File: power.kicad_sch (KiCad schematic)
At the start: 20 parts, among them J1 1054500101, J2 S2B-PH-SM4-TB, U3 BQ25601, U4 XC6210B332MR, U5 XC6210B182MR

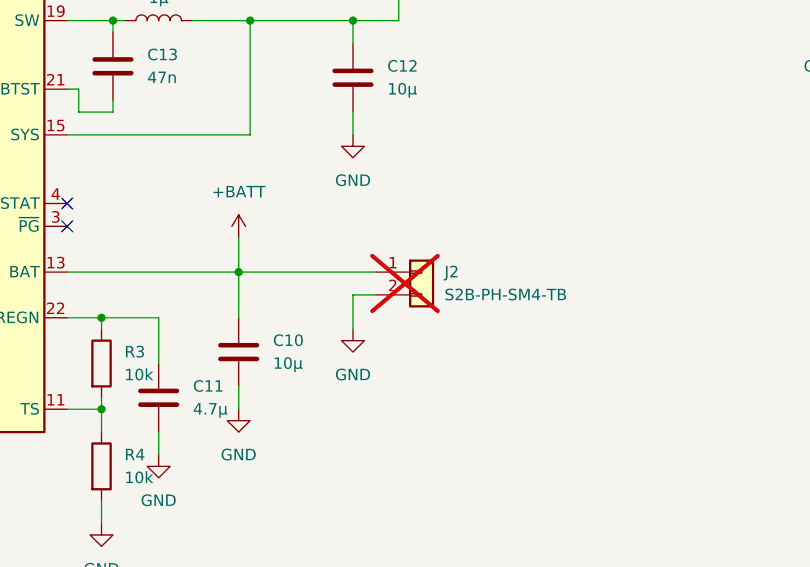
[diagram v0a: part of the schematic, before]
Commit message: Add battery connecter
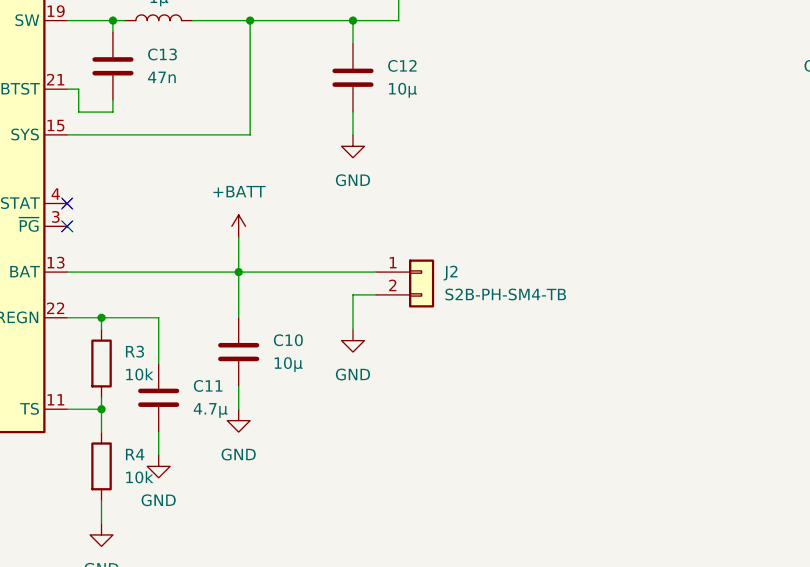
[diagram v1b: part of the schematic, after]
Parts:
- J2: JLCPCB Part # (none) -> C295747; manf# (none) -> S2B-PH-SM4-TB; now fitted; now in the parts list
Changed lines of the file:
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@@
 			)
 		)
+		(property "Sim.Enable" ""
+			(at 209.55 96.52 0)
+			(effects
+				(font
+					(size 1.27 1.27)
+				)
+				(hide yes)
+			)
+		)
 		(pin "3"
 		)
@@
 			)
 		)
+		(property "Sim.Enable" ""
+			(at 132.08 114.3 0)
+			(effects
+				(font
+					(size 1.27 1.27)
+				)
+				(hide yes)
+			)
+		)
 		(pin "2"
 		)
@@
 			)
 		)
+		(property "Sim.Enable" ""
+			(at 95.25 52.07 0)
+			(effects
+				(font
+					(size 1.27 1.27)
+				)
+				(hide yes)
+			)
+		)
 		(pin "1"
 		)
@@
 			)
 		)
+		(property "Sim.Enable" ""
+			(at 182.88 58.42 0)
+			(effects
+				(font
+					(size 1.27 1.27)
+				)
+				(hide yes)
+			)
+		)
 		(pin "2"
 		)
@@
 			)
 		)
+		(property "Sim.Enable" ""
+			(at 119.38 144.78 0)
+			(effects
+				(font
+					(size 1.27 1.27)
+				)
+				(hide yes)
+			)
+		)
 		(pin "2"
 		)
@@
 			)
 		)
+		(property "Sim.Enable" ""
+			(at 104.14 146.05 0)
+			(effects
+				(font
+					(size 1.27 1.27)
+				)
+				(hide yes)
+			)
+		)
 		(pin "2"
 		)
@@
 			)
 		)
+		(property "Sim.Enable" ""
+			(at 87.63 130.81 0)
+			(effects
+				(font
+					(size 1.27 1.27)
+				)
+				(hide yes)
+			)
+		)
 		(pin "1"
 		)
@@
 			)
 		)
+		(property "Sim.Enable" ""
+			(at 228.6 100.33 0)
+			(effects
+				(font
+					(size 1.27 1.27)
+				)
+				(hide yes)
+			)
+		)
 		(pin "2"
 		)
@@
 			)
 		)
+		(property "Sim.Enable" ""
+			(at 110.49 149.86 0)
+			(effects
+				(font
+					(size 1.27 1.27)
+				)
+				(hide yes)
+			)
+		)
 		(pin "2"
 		)
@@
 			)
 		)
+		(property "Sim.Enable" ""
+			(at 104.14 52.07 0)
+			(effects
+				(font
+					(size 1.27 1.27)
+				)
+				(hide yes)
+			)
+		)
 		(pin "1"
 		)
@@
 			)
 		)
+		(property "Sim.Enable" ""
+			(at 105.41 113.03 0)
+			(effects
+				(font
+					(size 1.27 1.27)
+				)
+				(hide yes)
+			)
+		)
 		(pin "2"
 		)
@@
 			)
 		)
+		(property "Sim.Enable" ""
+			(at 110.49 107.95 90)
+			(effects
+				(font
+					(size 1.27 1.27)
+				)
+				(hide yes)
+			)
+		)
 		(pin "1"
 		)
@@
 			)
 		)
+		(property "Sim.Enable" ""
+			(at 184.15 101.6 0)
+			(effects
+				(font
+					(size 1.27 1.27)
+				)
+				(hide yes)
+			)
+		)
 		(pin "2"
 		)
@@
 			)
 		)
+		(property "Sim.Enable" ""
+			(at 208.28 53.34 0)
+			(effects
+				(font
+					(size 1.27 1.27)
+				)
+				(hide yes)
+			)
+		)
 		(pin "3"
 		)
@@
 			)
 		)
+		(property "Sim.Enable" ""
+			(at 48.26 116.84 0)
+			(effects
+				(font
+					(size 1.27 1.27)
+				)
+				(hide yes)
+			)
+		)
 		(pin "2"
 		)
@@
 		(unit 1)
 		(exclude_from_sim no)
-		(in_bom no)
+		(in_bom yes)
 		(on_board yes)
-		(dnp yes)
+		(dnp no)
 		(fields_autoplaced yes)
 		(property "Reference" "J2"
@@
 			)
 		)
-		(property "JLCPCB Part #" ""
+		(property "JLCPCB Part #" "C295747"
 			(at 139.7 135.89 0)
 			(effects
@@
 			)
 		)
+		(property "Sim.Enable" ""
+			(at 139.7 135.89 0)
+			(effects
+				(font
+					(size 1.27 1.27)
+				)
+				(hide yes)
+			)
+		)
+		(property "manf#" "S2B-PH-SM4-TB"
+			(at 139.7 135.89 0)
+			(effects
+				(font
+					(size 1.27 1.27)
+				)
+				(hide yes)
+			)
+		)
 		(pin "1"
 		)
@@
 			)
 		)
+		(property "Sim.Enable" ""
+			(at 227.33 57.15 0)
+			(effects
+				(font
+					(size 1.27 1.27)
+				)
+				(hide yes)
+			)
+		)
 		(pin "2"
 		)
@@
 			)
 		)
+		(property "Sim.Enable" ""
+			(at 53.34 48.26 0)
+			(effects
+				(font
+					(size 1.27 1.27)
+				)
+				(hide yes)
+			)
+		)
 		(pin "S1"
 		)
@@
 			)
 		)
+		(property "Sim.Enable" ""
+			(at 104.14 157.48 0)
+			(effects
+				(font
+					(size 1.27 1.27)
+				)
+				(hide yes)
+			)
+		)
 		(pin "2"
 		)
@@
 			(at 66.04 157.48 0)
 			(effects
+				(font
+					(size 1.27 1.27)
+				)
+				(hide yes)
+			)
+		)
+		(property "Sim.Enable" ""
+			(at 66.04 157.48 0)
+			(effects

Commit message: some PCB correction
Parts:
- J1: value 1054500101 -> GT-USB-7025; JLCPCB Part # C134092 -> C27636760; manf# 1054500101 -> 12402012E212A
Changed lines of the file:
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@@
 	(wire
 		(pts
+			(xy 53.34 71.12) (xy 53.34 74.93)
+		)
+		(stroke
+			(width 0)
+			(type default)
+		)
+	)
+	(wire
+		(pts
 			(xy 190.5 50.8) (xy 182.88 50.8)
 		)
@@
 	(wire
 		(pts
-			(xy 53.34 71.12) (xy 53.34 74.93)
-		)
-		(stroke
-			(width 0)
-			(type default)
-		)
-	)
-	(wire
-		(pts
 			(xy 132.08 138.43) (xy 132.08 142.24)
 		)
@@
 			)
 		)
-		(property "Sim.Enable" ""
-			(at 209.55 96.52 0)
-			(effects
-				(font
-					(size 1.27 1.27)
-				)
-				(hide yes)
-			)
-		)
 		(pin "3"
 		)
@@
 			)
 		)
-		(property "Sim.Enable" ""
-			(at 132.08 114.3 0)
-			(effects
-				(font
-					(size 1.27 1.27)
-				)
-				(hide yes)
-			)
-		)
 		(pin "2"
 		)
@@
 			)
 		)
-		(property "Sim.Enable" ""
-			(at 95.25 52.07 0)
-			(effects
-				(font
-					(size 1.27 1.27)
-				)
-				(hide yes)
-			)
-		)
 		(pin "1"
 		)
@@
 			)
 		)
-		(property "Sim.Enable" ""
-			(at 182.88 58.42 0)
-			(effects
-				(font
-					(size 1.27 1.27)
-				)
-				(hide yes)
-			)
-		)
 		(pin "2"
 		)
@@
 			)
 		)
-		(property "Sim.Enable" ""
-			(at 119.38 144.78 0)
-			(effects
-				(font
-					(size 1.27 1.27)
-				)
-				(hide yes)
-			)
-		)
 		(pin "2"
 		)
@@
 			)
 		)
-		(property "Sim.Enable" ""
-			(at 104.14 146.05 0)
-			(effects
-				(font
-					(size 1.27 1.27)
-				)
-				(hide yes)
-			)
-		)
 		(pin "2"
 		)
@@
 			)
 		)
-		(property "Sim.Enable" ""
-			(at 87.63 130.81 0)
-			(effects
-				(font
-					(size 1.27 1.27)
-				)
-				(hide yes)
-			)
-		)
 		(pin "1"
 		)
@@
 			)
 		)
-		(property "Sim.Enable" ""
-			(at 228.6 100.33 0)
-			(effects
-				(font
-					(size 1.27 1.27)
-				)
-				(hide yes)
-			)
-		)
 		(pin "2"
 		)
@@
 			)
 		)
-		(property "Sim.Enable" ""
-			(at 110.49 149.86 0)
-			(effects
-				(font
-					(size 1.27 1.27)
-				)
-				(hide yes)
-			)
-		)
 		(pin "2"
 		)
@@
 			)
 		)
-		(property "Sim.Enable" ""
-			(at 104.14 52.07 0)
-			(effects
-				(font
-					(size 1.27 1.27)
-				)
-				(hide yes)
-			)
-		)
 		(pin "1"
 		)
@@
 			)
 		)
-		(property "Sim.Enable" ""
-			(at 105.41 113.03 0)
-			(effects
-				(font
-					(size 1.27 1.27)
-				)
-				(hide yes)
-			)
-		)
 		(pin "2"
 		)
@@
 			)
 		)
-		(property "Sim.Enable" ""
-			(at 110.49 107.95 90)
-			(effects
-				(font
-					(size 1.27 1.27)
-				)
-				(hide yes)
-			)
-		)
 		(pin "1"
 		)
@@
 			)
 		)
-		(property "Sim.Enable" ""
-			(at 184.15 101.6 0)
-			(effects
-				(font
-					(size 1.27 1.27)
-				)
-				(hide yes)
-			)
-		)
 		(pin "2"
 		)
@@
 			)
 		)
-		(property "Sim.Enable" ""
-			(at 208.28 53.34 0)
-			(effects
-				(font
-					(size 1.27 1.27)
-				)
-				(hide yes)
-			)
-		)
 		(pin "3"
 		)
@@
 			)
 		)
-		(property "Sim.Enable" ""
-			(at 48.26 116.84 0)
-			(effects
-				(font
-					(size 1.27 1.27)
-				)
-				(hide yes)
-			)
-		)
 		(pin "2"
 		)
@@
 			)
 		)
-		(property "Sim.Enable" ""
-			(at 139.7 135.89 0)
-			(effects
-				(font
-					(size 1.27 1.27)
-				)
-				(hide yes)
-			)
-		)
 		(property "manf#" "S2B-PH-SM4-TB"
 			(at 139.7 135.89 0)
@@
 			)
 		)
-		(property "Sim.Enable" ""
-			(at 227.33 57.15 0)
-			(effects
-				(font
-					(size 1.27 1.27)
-				)
-				(hide yes)
-			)
-		)
 		(pin "2"
 		)
@@
 			)
 		)
-		(property "Value" "1054500101"
+		(property "Value" "GT-USB-7025"
 			(at 53.34 27.94 0)
 			(effects
@@
 			)
 		)
-		(property "manf#" "1054500101"
+		(property "manf#" "12402012E212A"
 			(at 53.34 48.26 0)
 			(effects
@@
 			)
 		)
-		(property "JLCPCB Part #" "C134092"
+		(property "JLCPCB Part #" "C27636760"
 			(at 53.34 48.26 0)
 			(effects
@@
 			)
 		)
-		(property "Sim.Enable" ""
-			(at 53.34 48.26 0)
-			(effects
-				(font
-					(size 1.27 1.27)
-				)
-				(hide yes)
-			)
-		)
 		(pin "S1"
 		)
@@
 			)
 		)
-		(property "Sim.Enable" ""
-			(at 104.14 157.48 0)
-			(effects
-				(font
-					(size 1.27 1.27)
-				)
-				(hide yes)
-			)
-		)
 		(pin "2"
 		)
@@
 			(at 66.04 157.48 0)
 			(effects
-				(font
-					(size 1.27 1.27)
-				)
-				(hide yes)
-			)
-		)
-		(property "Sim.Enable" ""
-			(at 66.04 157.48 0)
-			(effects
